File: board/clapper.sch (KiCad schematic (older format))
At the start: 29 parts

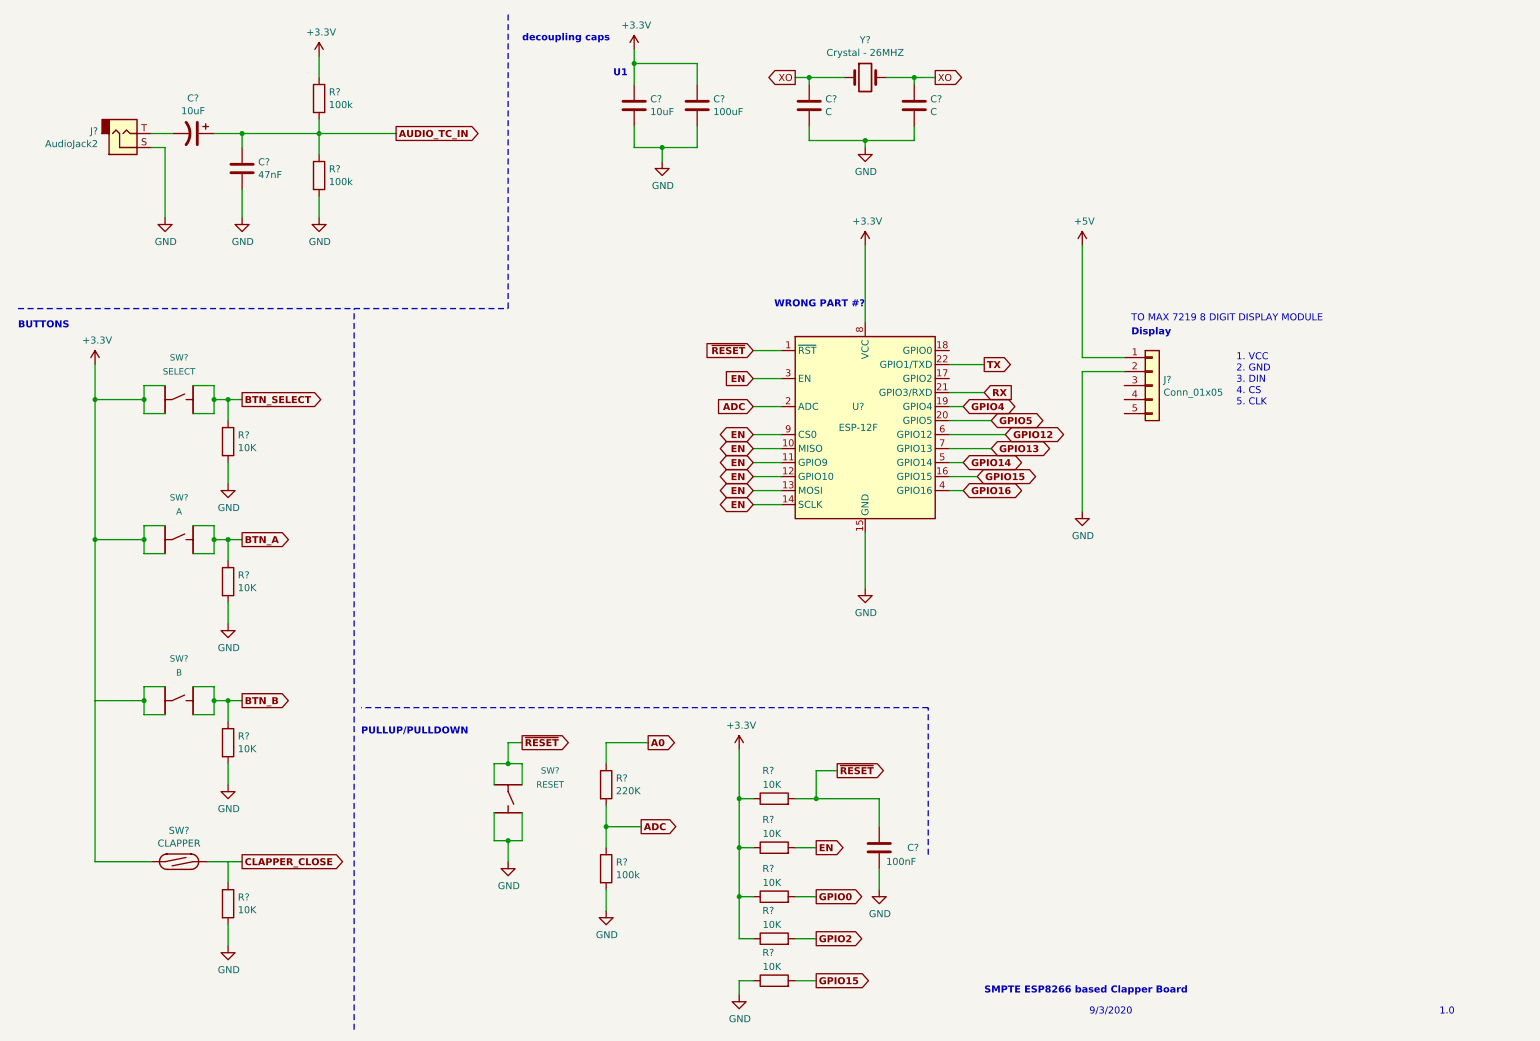
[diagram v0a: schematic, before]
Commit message: clean up dirs and check in code before rewriting timers
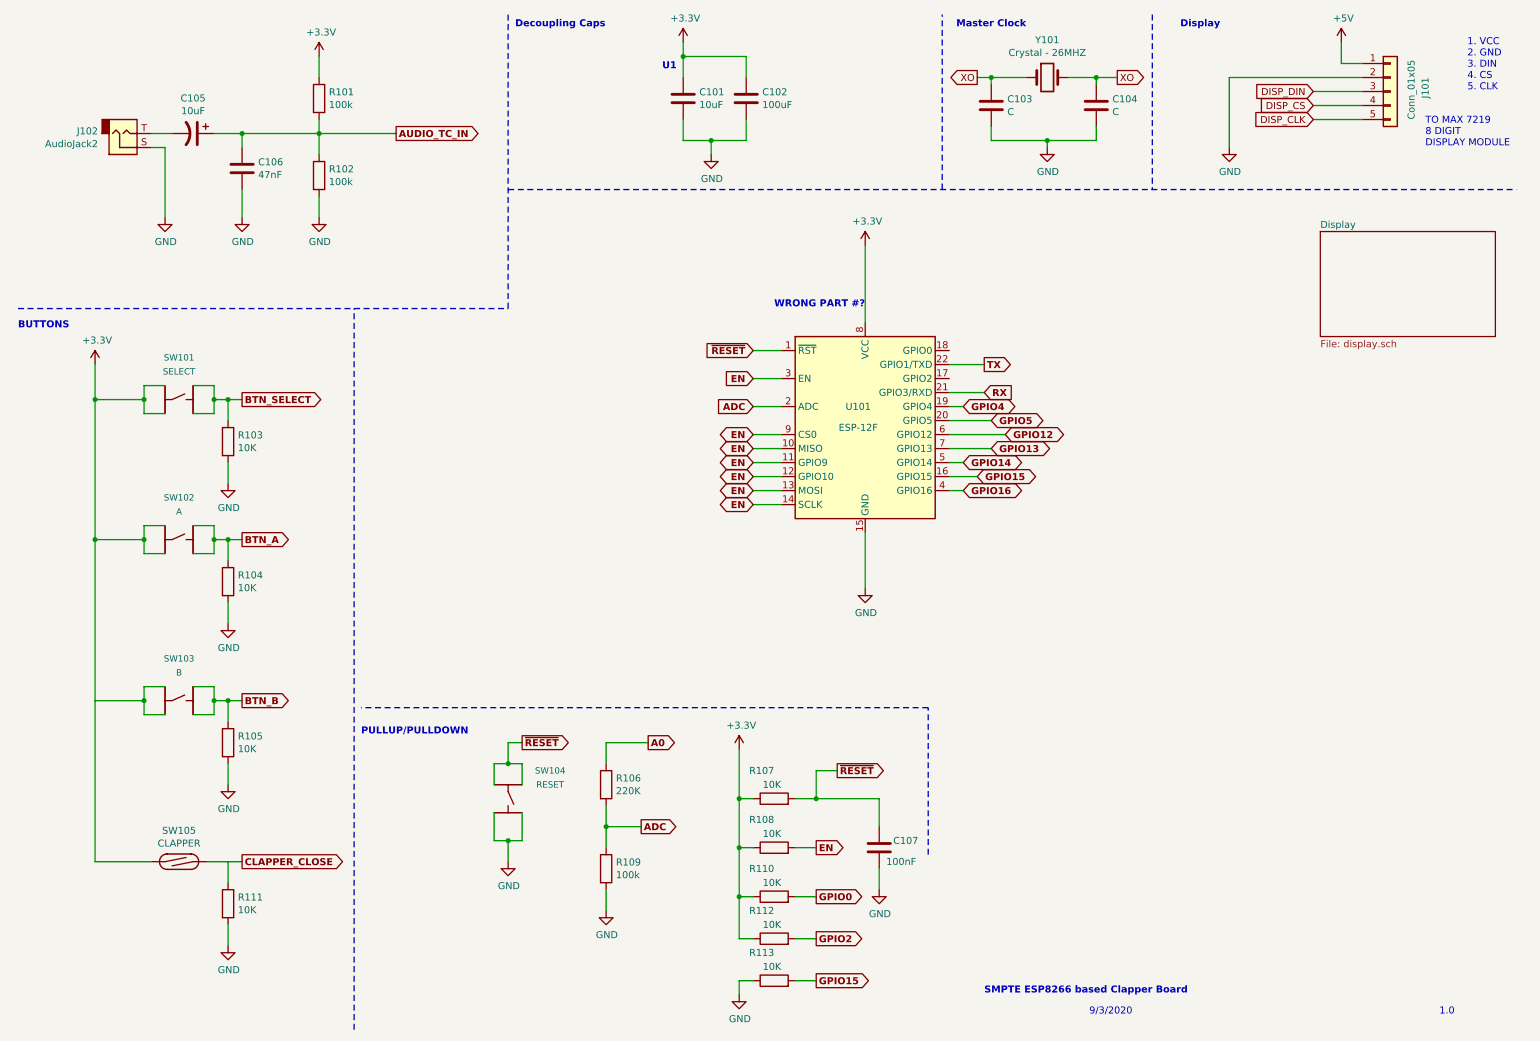
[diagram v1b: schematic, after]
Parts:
- gave numbers to parts that had none: 29
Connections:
- net DISP_DIN: now reaches J101.3 (Pin_3)
- net DISP_CS: now reaches J101.4 (Pin_4)
- net DISP_CLK: now reaches J101.5 (Pin_5)
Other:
- note added: "Decoupling Caps\n"
- note added: "Master Clock\n"
- note added: "TO MAX 7219 \n8 DIGIT \nDISPLAY MODULE\n"
- note removed: "TO MAX 7219 8 DIGIT DISPLAY MODULE\n"
- note removed: "decoupling caps\n"
- moved on the sheet: C101, C102, C103, C104, J101, Y101

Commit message: Update board with tested audio input circuit. Add in the 'feed' menu option.
Update readme
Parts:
- removed C106: 47nF, symbol Device:C
- removed R101, R102: 100k, symbol Device:R
- added D?: BAT54, symbol Device:D_Schottky
- added Q? (x2): PN2222A, Package_TO_SOT_THT:TO-92_Inline, symbol Transistor_BJT:PN2222A
- added R? (x3): 10k, symbol Device:R
- added TP?: TC_COND_IN, symbol Connector:TestPoint
- added TP?: TC_AUDIO_IN, symbol Connector:TestPoint
- added TP?: TC_DATA_IN, symbol Connector:TestPoint
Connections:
- net AUDIO_TC_IN is gone; now on an unnamed net: C105.1
- net +3V3: now also R?.2, R?.2
- net GND: now also D?.2 (A), Q?.1 (E), Q?.1 (E)
- net at J102.T: now also TP?.1; no longer C105.2
- new net: C105.2, R?.2
- new net: D?.1 (K), Q?.2 (B), R?.1, TP?.1
- new net: Q?.2 (B), Q?.3 (C), R?.1
- new net TC_IN: Q?.3 (C), R?.1, TP?.1
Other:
- note added: "AUDIO INPUT (1-BIT ADC)"
- note added: "TODO:\n\nBATTERY PLUG AND USB CHARGER (SAME AS DC27 BADGE)\nOUTPUT DIFFERENTIAL AMPLIFIER\n\nCHECK ALL PINS\n"
- moved on the sheet: C105, J102

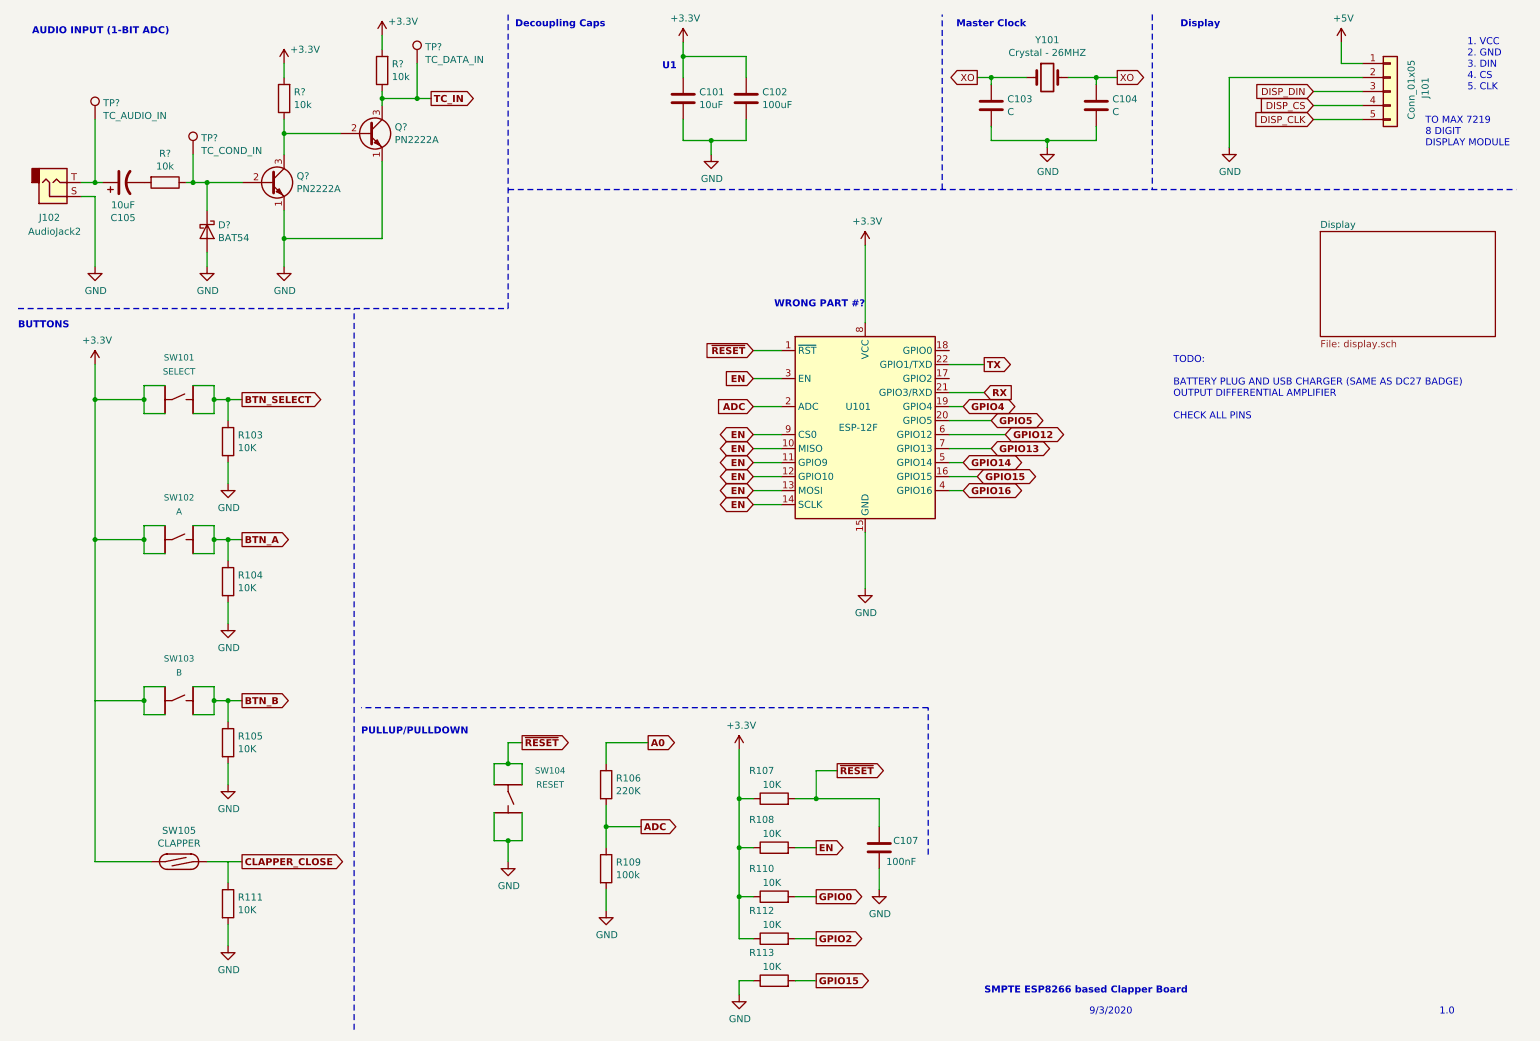
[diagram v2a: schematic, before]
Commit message: update schematic with switches, fix up default config
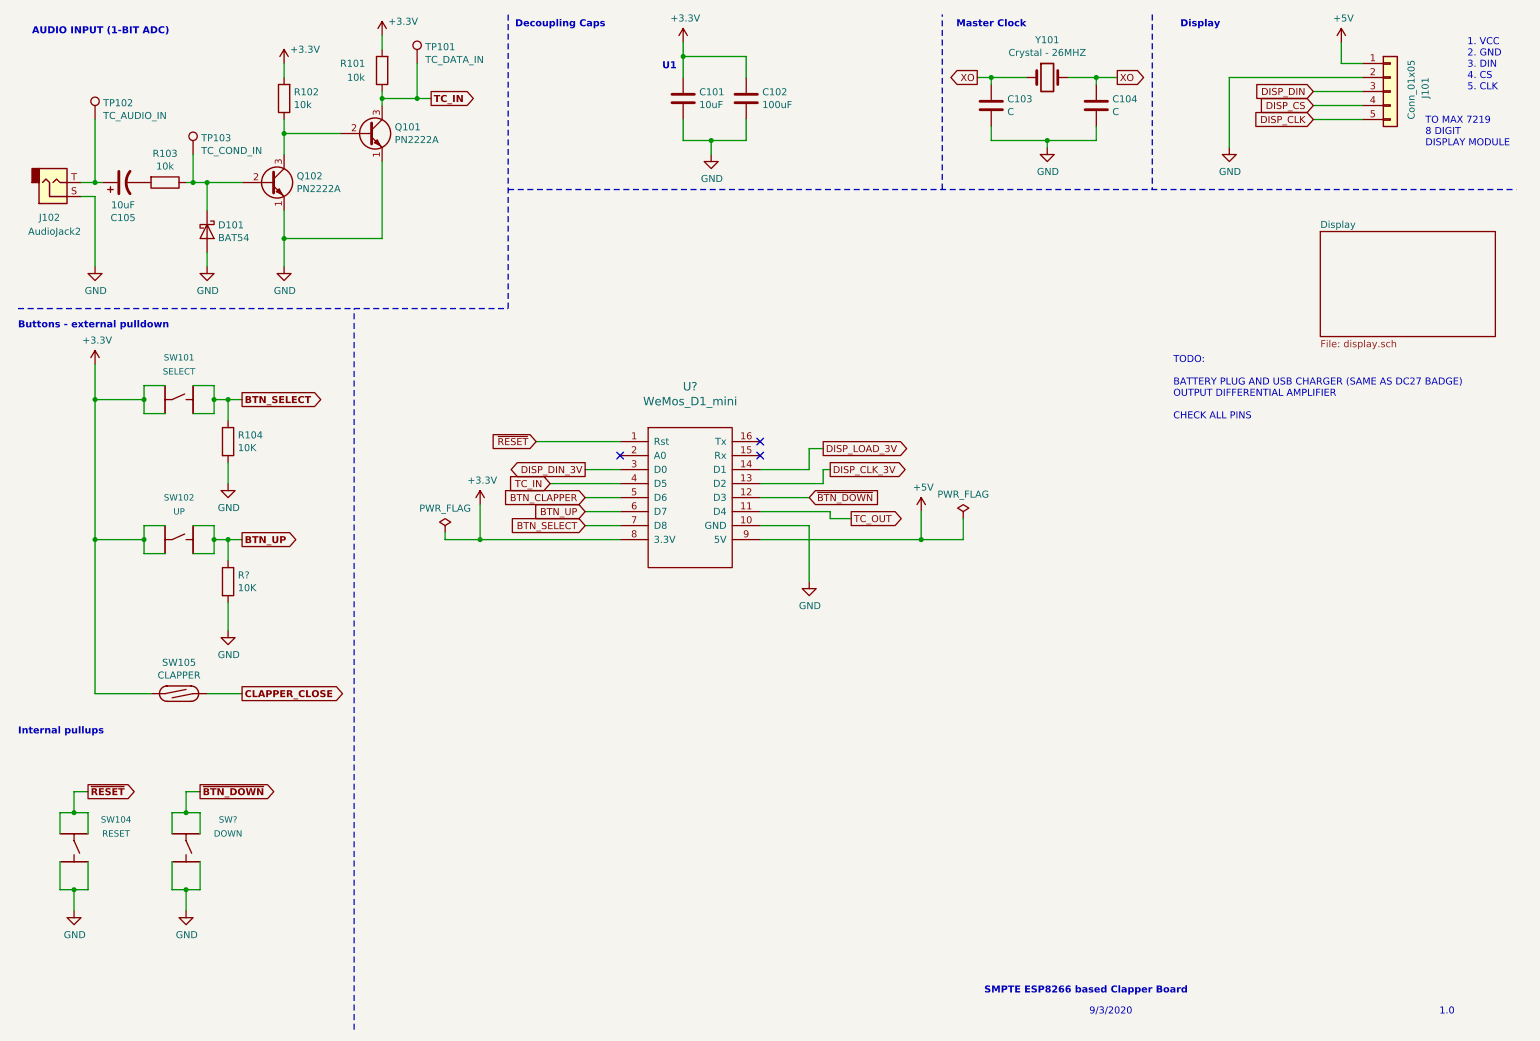
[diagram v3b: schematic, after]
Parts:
- removed C107: 100nF, symbol Device:C
- removed R104, R105, R107, R108, R110, R111, R112, R113: 10K, symbol Device:R
- removed R106: 220K, symbol Device:R
- removed R109: 100k, symbol Device:R
- removed SW103: B, MF_Switches_TACT6MM, symbol MF_Switches:TACT_6MM
- removed U101: ESP-12F, RF_Module:ESP-12E, symbol RF_Module:ESP-12F
- added R?: 10K, symbol Device:R
- added SW?: DOWN, MF_Switches_TACT6MM, symbol MF_Switches:TACT_6MM
- added U?: WeMos_D1_mini, symbol wemos_mini:WeMos_D1_mini
- SW102: value A -> UP
- gave numbers to parts that had none: 9
- renumbered R103 to R104
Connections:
- net +3V3: now also U?.8 (3.3V)
- net +5V: now also U?.9 (5V)
- net BTN_SELECT: now also U?.7 (D8)
- net GND: now also R?.2, SW?.P$1, SW?.P$2, U?.10 (GND)
- net TC_IN: now also U?.4 (D5)
- net ~RESET: now also U?.1 (Rst)
- net BTN_A renamed BTN_UP
- net BTN_UP: now also R?.1, U?.6 (D7)
- new net BTN_CLAPPER: U?.5 (D6)
- new net DISP_CLK_3V: U?.13 (D2)
- new net DISP_DIN_3V: U?.3 (D0)
- new net DISP_LOAD_3V: U?.14 (D1)
- new net TC_OUT: U?.11 (D4)
- new net ~BTN_DOWN: SW?.P$3, SW?.P$4, U?.12 (D3)
- no-connect marks 0 -> 3
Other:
- note added: "Buttons - external pulldown"
- note added: "Internal pullups\n"
- note removed: "BUTTONS\n"
- note removed: "PULLUP/PULLDOWN\n"
- note removed: "WRONG PART #?\n"
- moved on the sheet: SW104, SW105

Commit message: Switch board over to using a0 for clapper input and add voltage divider. This frees up a pin for timecode output.
always increment the clock regardless of internal setting (clock
generation tbd)
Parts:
- removed C101: 10uF, symbol Device:C
- removed C102: 100uF, symbol Device:C
- removed C103, C104: C, symbol Device:C
- removed Y101: Crystal - 26MHZ, symbol Device:Crystal
- added R?: 2300, symbol Device:R
- added R?: 1000, symbol Device:R
- renumbered Q102 to Q101, Q101 to Q102
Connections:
- net CLAPPER_CLOSE is gone; now on net BTN_CLAPPER: SW105.1
- net +3V3: now also R?.1; no longer SW105.2
- net GND: now also R?.2
- new net: R?.1, R?.2, SW105.2
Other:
- note added: "1.0V Divider\nOutput\n"
- note added: "D101 in Original design\nwas a 1N4001"
- note added: "On a High, Q101\npulls the circuit low"
- note added: "Q102 acts as a NOT gate"
- note added: "We need a clean digital pin as an output. \n\nMaybe we should move the clapper pin to A0, \nbecause otherwise we are out of pins.\n"
- note removed: "Decoupling Caps\n"
- note removed: "Master Clock\n"
- note removed: "U1\n"
- moved on the sheet: SW104, SW?
